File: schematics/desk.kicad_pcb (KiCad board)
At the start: 2 copper layers, 70 x 100 mm, 38 parts, among them K1 energized = UP (raises desk), K2 energized = DOWN (lowers desk), Q1 IRLZ44N, Q2 2N7000, Q3 2N7000, Q4 BC337, Q5 BC327, U1 LM2596HV 29V-5V, U2 ESP32_DevKitC, U3 74HC123 250ms, U5 ACS724xLCTR-05AB, U6 74HC08

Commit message: Relocate TB3/TB4 and U2 for direct USB edge access
TB3+TB4 sat right against U2's USB-C end with only ~1mm clearance,
and blocked any enclosure opening from reaching it. Both terminals are
now fully internal (wired via pigtail before the enclosure is
mounted), so their position is no longer tied to a specific board
edge - moved them to a free pocket lower on the right side.

That freed the space to also shift U2 itself right so the USB-C end
sits ~1.4mm from the board's right edge (was ~11mm) for direct
enclosure access. As a side effect this pulls U2's antenna end fully
inside the board too, removing the previous edge overhang.

Re-routed from scratch after the moves; DRC clean against this
project's already-accepted categories (silkscreen overlaps, isolated-
copper islands, one starved thermal spoke) - no new clearance or
electrical issues.

Also fixed reroute_pcb.py's overlap check, which compared full
silkscreen-inclusive bounding boxes and would reject the many
silkscreen overlaps this board already accepts by design (irrelevant
for a self-milled board). It now checks F.Courtyard boxes only,
matching the real placement constraint.
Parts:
- moved TB4 32.5 mm to (64.3, 61.9)
- moved TB3 29.4 mm to (64.3, 46.3)
- moved U2 9.87 mm to (13.7, 40.3)
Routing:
- net GND: track 362.6 -> 310.2 mm
- net DIR_A: track 78.9 -> 109.0 mm, vias 0 -> 2
- net Net-(TB3-Pin_1): track 71.0 -> 40.9 mm
- net Net-(Q1-G): track 44.7 -> 69.2 mm
- net +5V: track 213.1 -> 232.8 mm, vias 3 -> 1
- net SW_DN: track 20.5 -> 39.0 mm
- net /WDOG: track 53.3 -> 69.9 mm, vias 0 -> 1
- net Net-(TB3-Pin_2): track 49.8 -> 35.6 mm, vias 1 -> 3
- net +3V3: track 110.8 -> 98.6 mm
- net SW_UP: track 29.4 -> 40.8 mm, vias 0 -> 1
- net ISENSE: track 92.6 -> 102.6 mm
- net KICK: track 19.7 -> 29.5 mm
- net PWM: track 89.0 -> 98.2 mm
- net /MRET: track 48.0 -> 57.0 mm
- net Net-(TB2-Pin_1): track 44.4 -> 46.9 mm
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
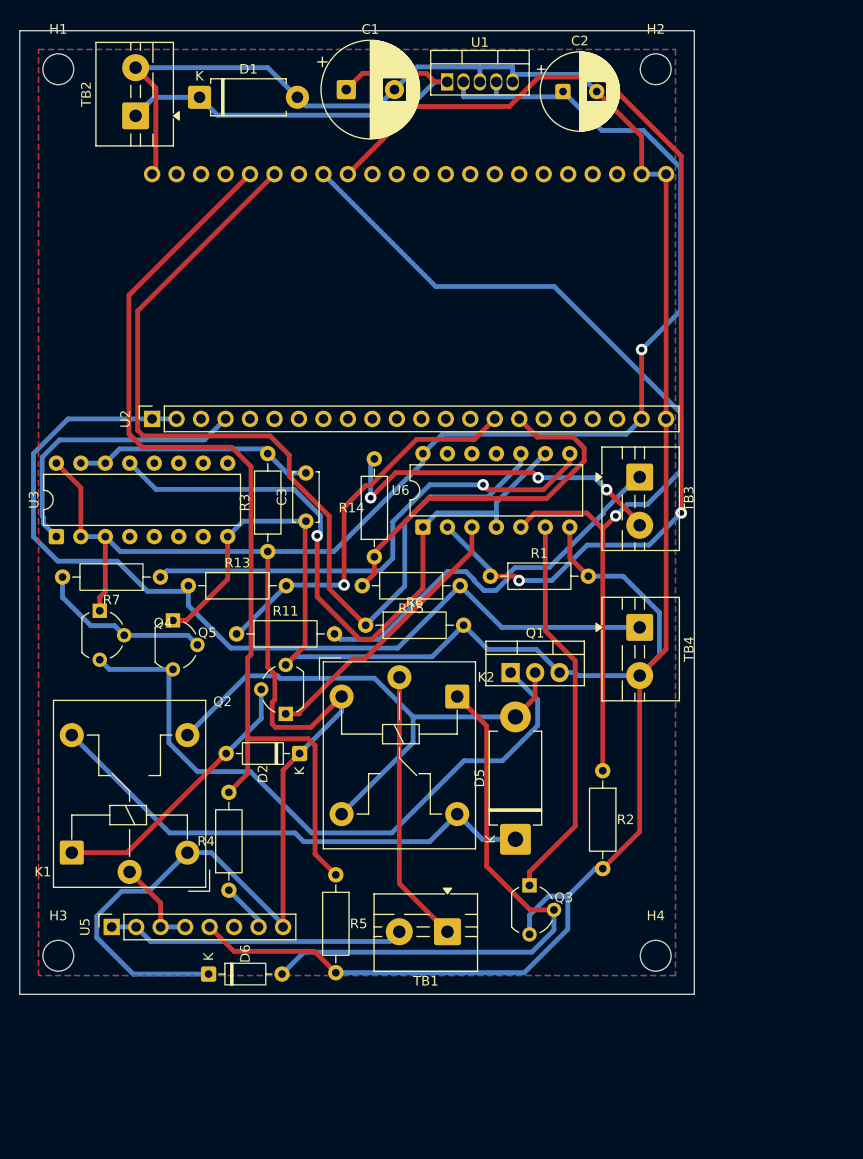
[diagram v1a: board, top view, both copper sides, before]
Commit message: Fix U2 courtyard, group TB1/TB2, and shorten Q3/R2 routes
U2's local footprint courtyard only modeled the pin-header envelope,
not the real devkit board - it missed the antenna (~7mm past the pin
envelope on one end) and the USB-C connector (~2.5mm on the other).
This let TB1/TB2 get placed directly under the antenna in an earlier
placement experiment with nothing to catch it. Extended the courtyard
in DevKitC_2x22_P2.54mm_1in_row.kicad_mod to cover both, and refreshed
U2 in the board from the corrected footprint.

With that real space accounted for, relocated TB1+TB2 to sit directly
side by side near the bottom edge (motor pair / supply pair), matching
that they already share a single external pigtail and have no other
placement constraint now that they're fully internal.

Q3 and R2 both route to U6 up near the board's middle; both were
sitting in the bottom-right corner near H4 for no reason tied to their
actual connections. Moved both closer to U6, which incidentally
dropped the board from 1 via to 0.

Re-routed and re-verified after each placement change; DRC clean
against this project's already-accepted categories (silkscreen
overlaps, isolated-copper islands, one starved thermal spoke).
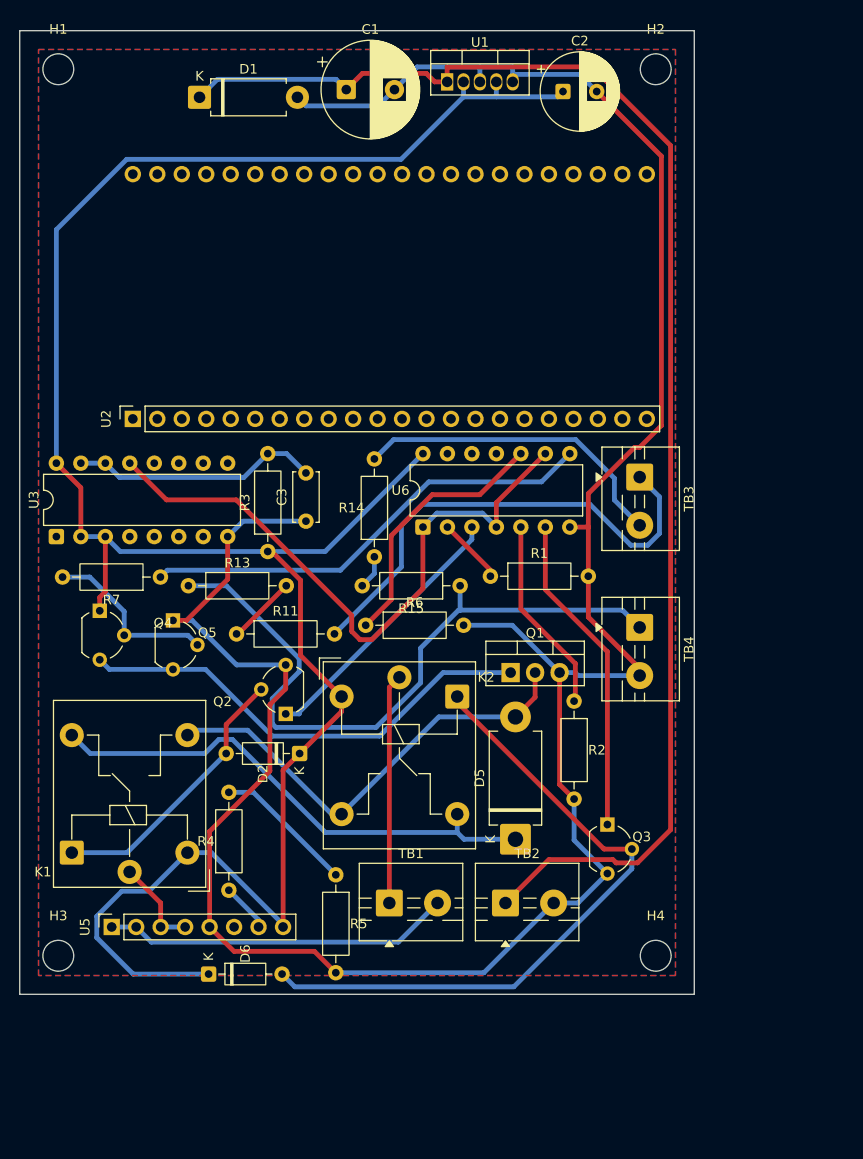
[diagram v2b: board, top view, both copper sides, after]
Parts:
- U2: value ESP32_DevKitC -> DevKitC_2x22_P2.54mm_1in_row
- moved TB2 90.3 mm to (50.4, 90.5), turned to 0 degrees
- moved Q3 10.3 mm to (61.0, 82.4)
- moved R2 7.81 mm to (57.5, 69.6)
- moved TB1 6.73 mm to (38.4, 90.5), turned to 0 degrees
- moved U2 2.00 mm to (11.7, 40.3)
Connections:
- U2 pad 1: +3V3 -> (no net)
- U2 pad 10: unconnected-(U2-GPIO17/ADC2_CH6-Pad10) -> (no net)
- U2 pad 11: unconnected-(U2-GPIO18/ADC2_CH7-Pad11) -> (no net)
- U2 pad 12: unconnected-(U2-GPIO8/ADC1_CH7-Pad12) -> (no net)
- U2 pad 13: unconnected-(U2-GPIO3/ADC1_CH2-Pad13) -> (no net)
- U2 pad 14: unconnected-(U2-GPIO46-Pad14) -> (no net)
- U2 pad 15: SW_UP -> (no net)
- U2 pad 16: SW_DN -> (no net)
- U2 pad 17: unconnected-(U2-GPIO11/ADC2_CH0-Pad17) -> (no net)
- U2 pad 18: SDA -> (no net)
- U2 pad 19: SCL -> (no net)
- U2 pad 2: +3V3 -> (no net)
- U2 pad 20: unconnected-(U2-GPIO14/ADC2_CH3-Pad20) -> (no net)
- U2 pad 21: +5V -> (no net)
- U2 pad 22: GND -> (no net)
- U2 pad 23: GND -> (no net)
- U2 pad 24: GND -> (no net)
- U2 pad 25: unconnected-(U2-GPIO19/USB_D--Pad25) -> (no net)
- U2 pad 26: unconnected-(U2-GPIO20/USB_D+-Pad26) -> (no net)
- U2 pad 27: unconnected-(U2-GPIO21-Pad27) -> (no net)
- U2 pad 28: unconnected-(U2-GPIO47-Pad28) -> (no net)
- U2 pad 29: unconnected-(U2-GPIO48-Pad29) -> (no net)
- U2 pad 3: unconnected-(U2-CHIP_PU-Pad3) -> (no net)
- U2 pad 30: unconnected-(U2-GPIO45-Pad30) -> (no net)
- U2 pad 31: unconnected-(U2-GPIO0-Pad31) -> (no net)
- U2 pad 32: unconnected-(U2-GPIO35-Pad32) -> (no net)
- U2 pad 33: unconnected-(U2-GPIO36-Pad33) -> (no net)
- U2 pad 34: unconnected-(U2-GPIO37-Pad34) -> (no net)
- U2 pad 35: unconnected-(U2-GPIO38-Pad35) -> (no net)
- U2 pad 36: DIR_A -> (no net)
- U2 pad 37: DIR_B -> (no net)
- U2 pad 38: unconnected-(U2-GPIO41/MTDI-Pad38) -> (no net)
- U2 pad 39: PWM -> (no net)
- U2 pad 4: KICK -> (no net)
- U2 pad 40: ISENSE -> (no net)
- U2 pad 41: unconnected-(U2-GPIO1/ADC1_CH0-Pad41) -> (no net)
- U2 pad 42: unconnected-(U2-GPIO44/U0RXD-Pad42) -> (no net)
- U2 pad 43: unconnected-(U2-GPIO43/U0TXD-Pad43) -> (no net)
- U2 pad 44: GND -> (no net)
- U2 pad 5: unconnected-(U2-GPIO5/ADC1_CH4-Pad5) -> (no net)
- U2 pad 6: unconnected-(U2-GPIO6/ADC1_CH5-Pad6) -> (no net)
- U2 pad 7: unconnected-(U2-GPIO7/ADC1_CH6-Pad7) -> (no net)
- U2 pad 8: unconnected-(U2-GPIO15/ADC2_CH4/32K_P-Pad8) -> (no net)
- U2 pad 9: unconnected-(U2-GPIO16/ADC2_CH5/32K_N-Pad9) -> (no net)
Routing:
- net DIR_A: track 109.0 -> 6.95 mm, vias 2 -> 0
- net Net-(TB2-Pin_1): track 46.9 -> 147.7 mm
- net ISENSE: track 102.6 -> 14.6 mm
- net DIR_B: track 98.8 -> 20.5 mm, vias 1 -> 0
- net PWM: track 98.2 -> 27.4 mm
- net GND: track 310.2 -> 263.5 mm
- net SW_DN: track 39.0 -> 3.52 mm
- net SW_UP: track 40.8 -> 7.23 mm, vias 1 -> 0
- net KICK: track 29.5 -> 0.00 mm
- net +3V3: track 98.6 -> 71.3 mm
- net Net-(Q1-G): track 69.2 -> 48.7 mm
- net Net-(TB3-Pin_1): track 40.9 -> 50.8 mm
- net /MRET: track 57.0 -> 47.5 mm
- net Net-(D6-A): track 59.9 -> 69.0 mm
- net Net-(Q3-G): track 40.4 -> 33.5 mm
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
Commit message: Drop the ACS724 Pololu carrier for a bare chip, draw the pigtail plugs, and clear the drawing-sheet border
ACS724 moves from the Pololu carrier to a bare SOIC-8 chip on a generic
SOIC-8-to-DIP-8 adapter. That drops two caps the carrier used to provide
for free - a 0.1uF VCC bypass and a 1nF FILTER-to-GND cap, both confirmed
against Allegro's own ACS712/ACS724 application circuit - so they're now
discrete parts on the main board (C4, C5), placed and routed. README,
SHOPPING_LIST.md and NETLIST.md are reconciled with the swap.

D1 goes back to a horizontal/laid-flat DO-15 mount now that the board has
room again, instead of the standing 2.54mm-pitch mount from the earlier
space crunch - easier to mount, and it drops D1's height off the board.

J2/J3 are now drawn as real parts: the pigtail's own Mini-Fit Jr plugs,
crimped onto the cable, distinct from J1/J4's fixed receptacles in the
motor housing/handset. Previously only J1/J4 were drawn, with TB1-4
connected to them purely by matching net-name labels and no literal
component in between - electrically fine, but understated what's
actually a real, separate, buy-and-crimp part. Both are on_board=False,
same as J1/J4/M1/PSU1.

The PCB board outline sat flush with the coordinate origin, which put it
running straight through the drawing sheet's default border margin in
any print/screenshot. Moved the whole board (outline, footprints,
tracks, zones, aux/grid origin) by a uniform +15/+15mm via pcbnew's own
board Move() - a rigid translation, no relative geometry changed - and
updated the handful of literal absolute-coordinate references in
enclosure/shell.scad (the two pigtail wall-hole centers, the USB slot)
to match. The mounting-hole positions are parametric and needed no
change. STL regenerated and re-rendered against the shifted board.

Also moved the aux/grid origin to H1's corner (was an arbitrary point
off the board entirely, left over from before the board was resized).
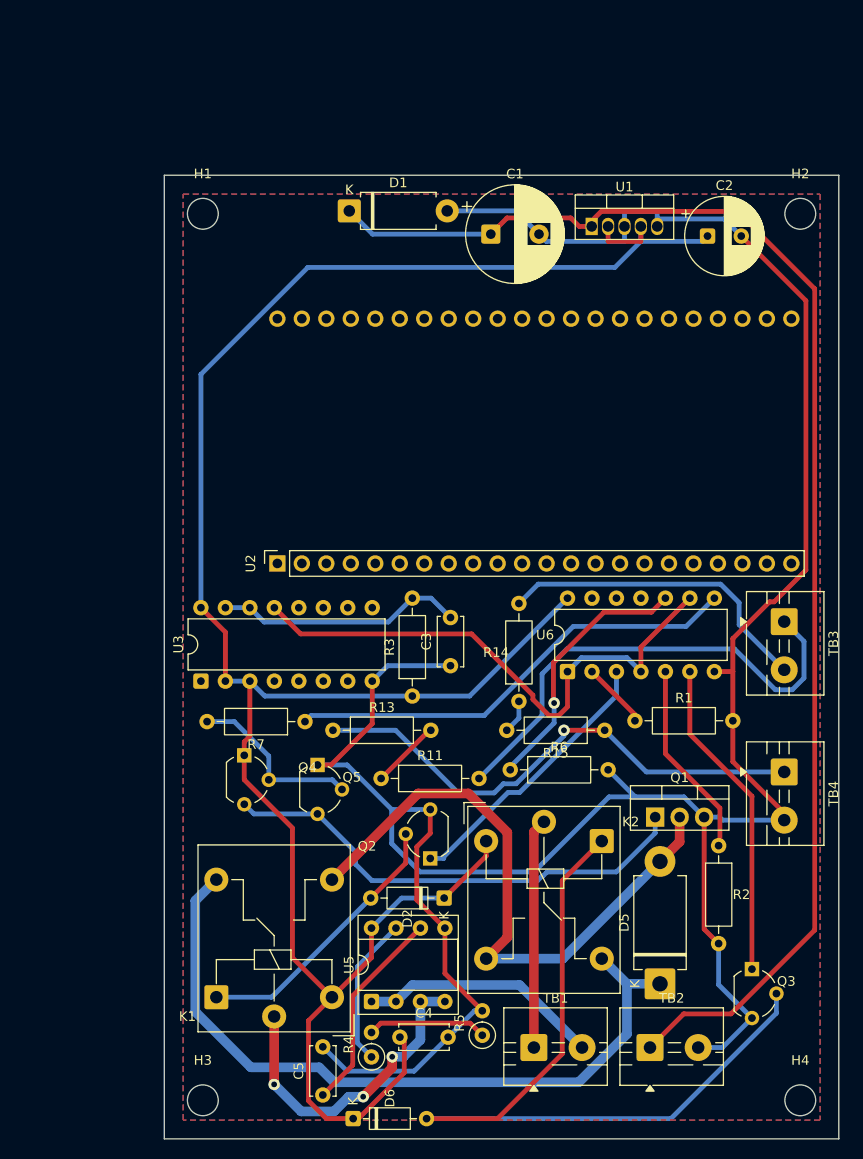
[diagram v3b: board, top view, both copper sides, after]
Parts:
- added C4: 100n, C_Disc_D5.0mm_W2.5mm_P5.00mm, F.Cu at (39.5, 104.5)
- added C5: 1n, C_Disc_D5.0mm_W2.5mm_P5.00mm, F.Cu at (31.4, 110.5)
- D1: footprint Diode_THT:D_DO-15_P10.16mm_Horizontal -> D_DO-15_P10.16mm_Horizontal
- R4, R5: footprint Resistor_THT:R_Axial_DIN0207_L6.3mm_D2.5mm_P10.16mm_Horizontal -> R_Axial_DIN0207_L6.3mm_D2.5mm_P2.54mm_Vertical
- U5: footprint Connector_PinSocket_2.54mm:PinSocket_1x08_P2.54mm_Vertical -> DIP-8_W7.62mm_Socket
- moved U5 28.0 mm to (36.5, 100.8)
- moved R4 22.8 mm to (36.5, 106.5)
- moved R5 22.5 mm to (48.0, 104.2), turned to 90 degrees
- moved C3 21.2 mm to (44.7, 65.9)
- moved R2 21.2 mm to (72.5, 84.6)
- moved C1 21.2 mm to (48.9, 21.1)
- moved C2 21.2 mm to (71.4, 21.3)
- moved D6 21.2 mm to (34.6, 112.9)
- moved H1 21.2 mm to (19.0, 19.0)
- moved H2 21.2 mm to (81.0, 19.0)
- moved H3 21.2 mm to (19.0, 111.0)
- moved H4 21.2 mm to (81.0, 111.0)
- moved K2 21.2 mm to (60.4, 84.1)
- moved Q2 21.2 mm to (42.6, 85.9)
- moved Q3 21.2 mm to (76.0, 97.4)
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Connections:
- U5 pad 6: unconnected-(U5-FILTER-Pad6) -> Net-(U5-FILTER)
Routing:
- net /DRV_UP: track 9.59 -> 33.7 mm, vias 0 -> 3
- net VSW: track 53.6 -> 76.9 mm
- net Net-(U5-FILTER): track 0.00 -> 21.5 mm
- net /MRET: track 47.5 -> 65.3 mm
- net +3V3: track 71.3 -> 54.4 mm, vias 0 -> 1
- net Net-(D6-A): track 69.0 -> 83.5 mm
- net Net-(TB1-Pin_2): track 36.1 -> 25.3 mm
- net Net-(U5-VIOUT): track 5.09 -> 15.6 mm
- net /WDOG: track 66.1 -> 57.9 mm
- net GND: track 263.5 -> 270.4 mm
- net Net-(TB2-Pin_1): track 147.7 -> 143.6 mm
- net ISENSE: track 14.6 -> 12.4 mm
- net +5V: track 228.5 -> 230.4 mm
- net Net-(Q1-G): track 48.7 -> 50.4 mm
- net Net-(Q2-G): track 28.2 -> 28.9 mm
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
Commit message: Fix TB pitch/ToF routing, renumber references, fix stale docs, implement read_current_()
- Fix TB1-5 footprint pitch to match the actually-ordered 2.54mm Degson
  part (board previously used a 5.00mm-pitch footprint)
- Add TB5 for a future ToF sensor's SDA/SCL, moved to GPIO38/41 after
  GPIO12/13 proved unroutable near U1's own margin; +3V3/GND for it
  shares TB2 instead of a dedicated terminal
- Renumber every reference designator (R/C/D/Q/U/TB/J/SW) to match
  schematic reading order, closing all numbering gaps
- Fix several stale references found along the way: leftover per-gate
  IC labels (U8/U9) in the relay-drive chain description, a fuse (F1)
  no longer fitted by design, "relay module" wording where this design
  drives coils directly, two incorrectly-laid-out ASCII diagrams (one
  showing SPDT switches with only 2 of 3 real terminals), and an ACS712
  sensitivity figure inconsistent with its actual datasheet spec
- Confirm §1.6's connector numbering against Molex's real SD-5557-003
  drawing instead of treating it as unverifiable
- Implement read_current_() for both ESP-IDF 4.x and 5.x; fix
  desk.yaml, which targeted the classic ESP32 instead of the S3 this
  design is built around (every GPIO number was consequently wrong)
- Strip SHOPPING_LIST.md down to a plain checklist
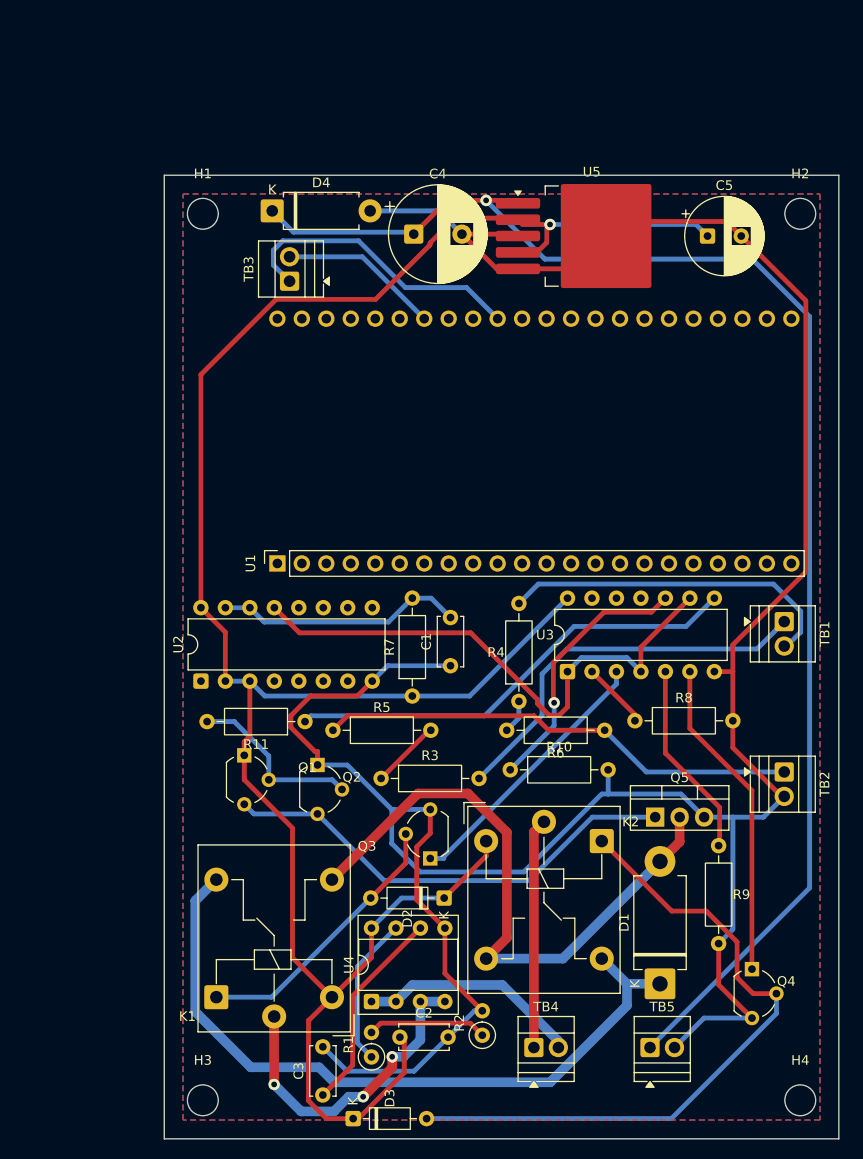
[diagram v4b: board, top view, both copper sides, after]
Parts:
- removed the U1 at (59.4, 20.3)
- added TB5: supply pair, TerminalBlock_Xinya_XY308-2.54-2P_1x02_P2.54mm_Horizontal, F.Cu at (65.4, 105.5)
- added U5: LM2576HVS-5.0 29V-5V, TO-263-5_TabPin3, F.Cu at (59.4, 21.3)
- TB1: value motor pair -> signal pair; footprint TerminalBlock:TerminalBlock_MaiXu_MX126-5.0-02P_1x02_P5.00mm -> TerminalBlock_Xinya_XY308-2.54-2P_1x02_P2.54mm_Horizontal
- TB2: value supply pair -> power pair; footprint TerminalBlock:TerminalBlock_MaiXu_MX126-5.0-02P_1x02_P5.00mm -> TerminalBlock_Xinya_XY308-2.54-2P_1x02_P2.54mm_Horizontal
- TB3: value signal pair -> ToF signal pair; footprint TerminalBlock:TerminalBlock_MaiXu_MX126-5.0-02P_1x02_P5.00mm -> TerminalBlock_Xinya_XY308-2.54-2P_1x02_P2.54mm_Horizontal
- TB4: value power pair -> motor pair; footprint TerminalBlock:TerminalBlock_MaiXu_MX126-5.0-02P_1x02_P5.00mm -> TerminalBlock_Xinya_XY308-2.54-2P_1x02_P2.54mm_Horizontal
- U4: renamed from U5; value ACS724xLCTR-05AB -> ACS712ELCTR-05B
- moved TB3 62.3 mm to (28.0, 26.0), turned to 90 degrees
- moved TB1 51.3 mm to (79.3, 61.3), turned to -90 degrees
- moved TB4 38.6 mm to (53.4, 105.5), turned to 0 degrees
- moved TB2 31.8 mm to (79.3, 76.9), turned to -90 degrees
- moved D4 8.00 mm to (26.2, 18.7)
- moved C4 8.00 mm to (40.9, 21.1)
- renumbered C3 to C1, C4 to C2, C5 to C3, C1 to C4, C2 to C5, D5 to D1, D6 to D3, D1 to D4, Q4 to Q1, Q5 to Q2, Q2 to Q3, Q3 to Q4, Q1 to Q5, R4 to R1, R6 to R10, R7 to R11, R5 to R2, R11 to R3, R14 to R4, R13 to R5, R15 to R6, R3 to R7, R1 to R8, R2 to R9, U2 to U1, U3 to U2, U6 to U3
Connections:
- TB1 pad 1: Net-(TB1-Pin_1) -> Net-(TB3-Pin_1)
- TB1 pad 2: Net-(TB1-Pin_2) -> Net-(TB3-Pin_2)
- TB2 pad 1: Net-(TB2-Pin_1) -> +3V3
- TB3 pad 1: Net-(TB3-Pin_1) -> SDA
- TB3 pad 2: Net-(TB3-Pin_2) -> SCL
- TB4 pad 1: +3V3 -> Net-(TB1-Pin_1)
- TB4 pad 2: GND -> Net-(TB1-Pin_2)
- U1 pad 35: (no net) -> SDA
- U1 pad 38: (no net) -> SCL
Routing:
- net SDA: track 0.00 -> 30.9 mm
- net SCL: track 0.00 -> 16.6 mm
- net GND: track 270.4 -> 286.6 mm
- net Net-(D6-A): track 83.5 -> 69.7 mm
- net Net-(TB3-Pin_1): track 50.8 -> 40.9 mm
- net Net-(TB2-Pin_1): track 143.6 -> 149.4 mm, vias 0 -> 1
- net +3V3: track 54.4 -> 49.9 mm, vias 1 -> 0
- net Net-(TB3-Pin_2): track 33.4 -> 35.7 mm
- net Net-(TB1-Pin_2): track 25.3 -> 23.2 mm
- net VSW: track 76.9 -> 75.1 mm
- net Net-(Q1-G): track 50.4 -> 48.7 mm
- net +5V: track 230.4 -> 229.2 mm, vias 0 -> 1
- net Net-(Q2-G): track 28.9 -> 28.2 mm
